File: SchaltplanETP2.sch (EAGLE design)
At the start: 62 parts, among them IC1 LM2674, IC2 ZXLD1350, IC3 ZXLD1350, IC4 ZXLD1350, IC5 ZXLD1350, M1 RN42_BLUETOOTH, T1 BUK98150-55A, X1 TERMINAL_BLOCK_MC000036, X2 TERMINAL_BLOCK_MC000036

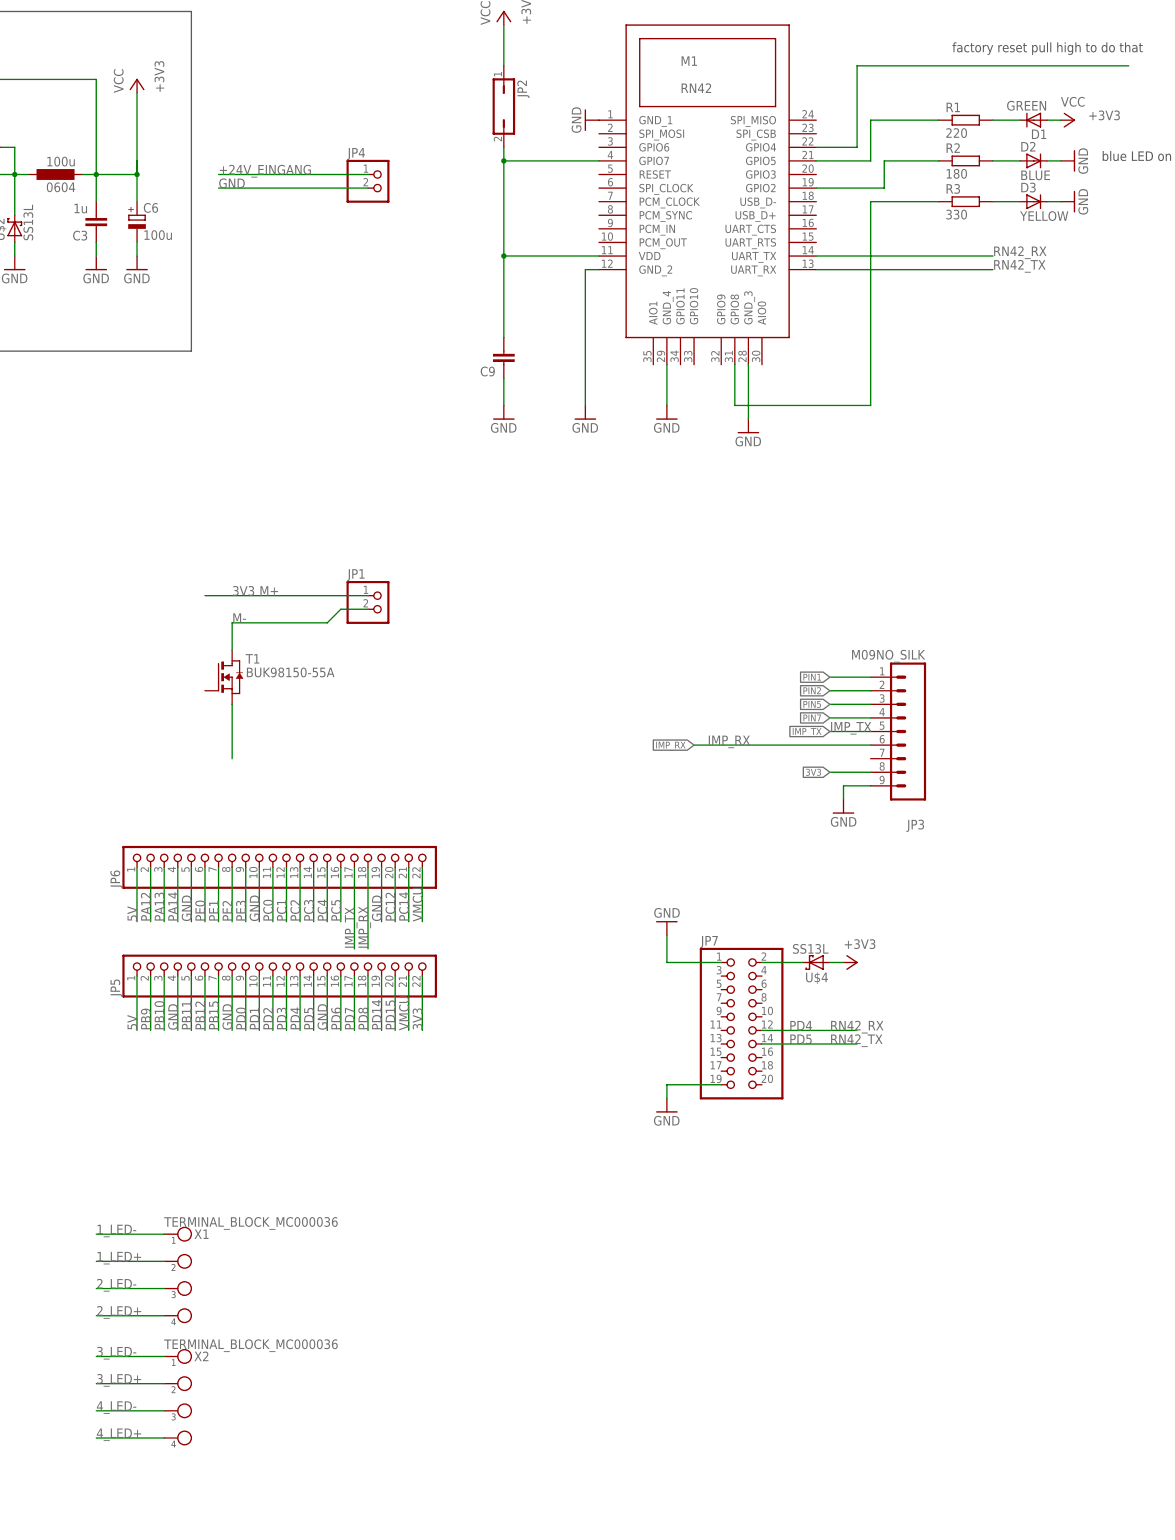
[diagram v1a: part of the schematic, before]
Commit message: connected leds directly to 24V
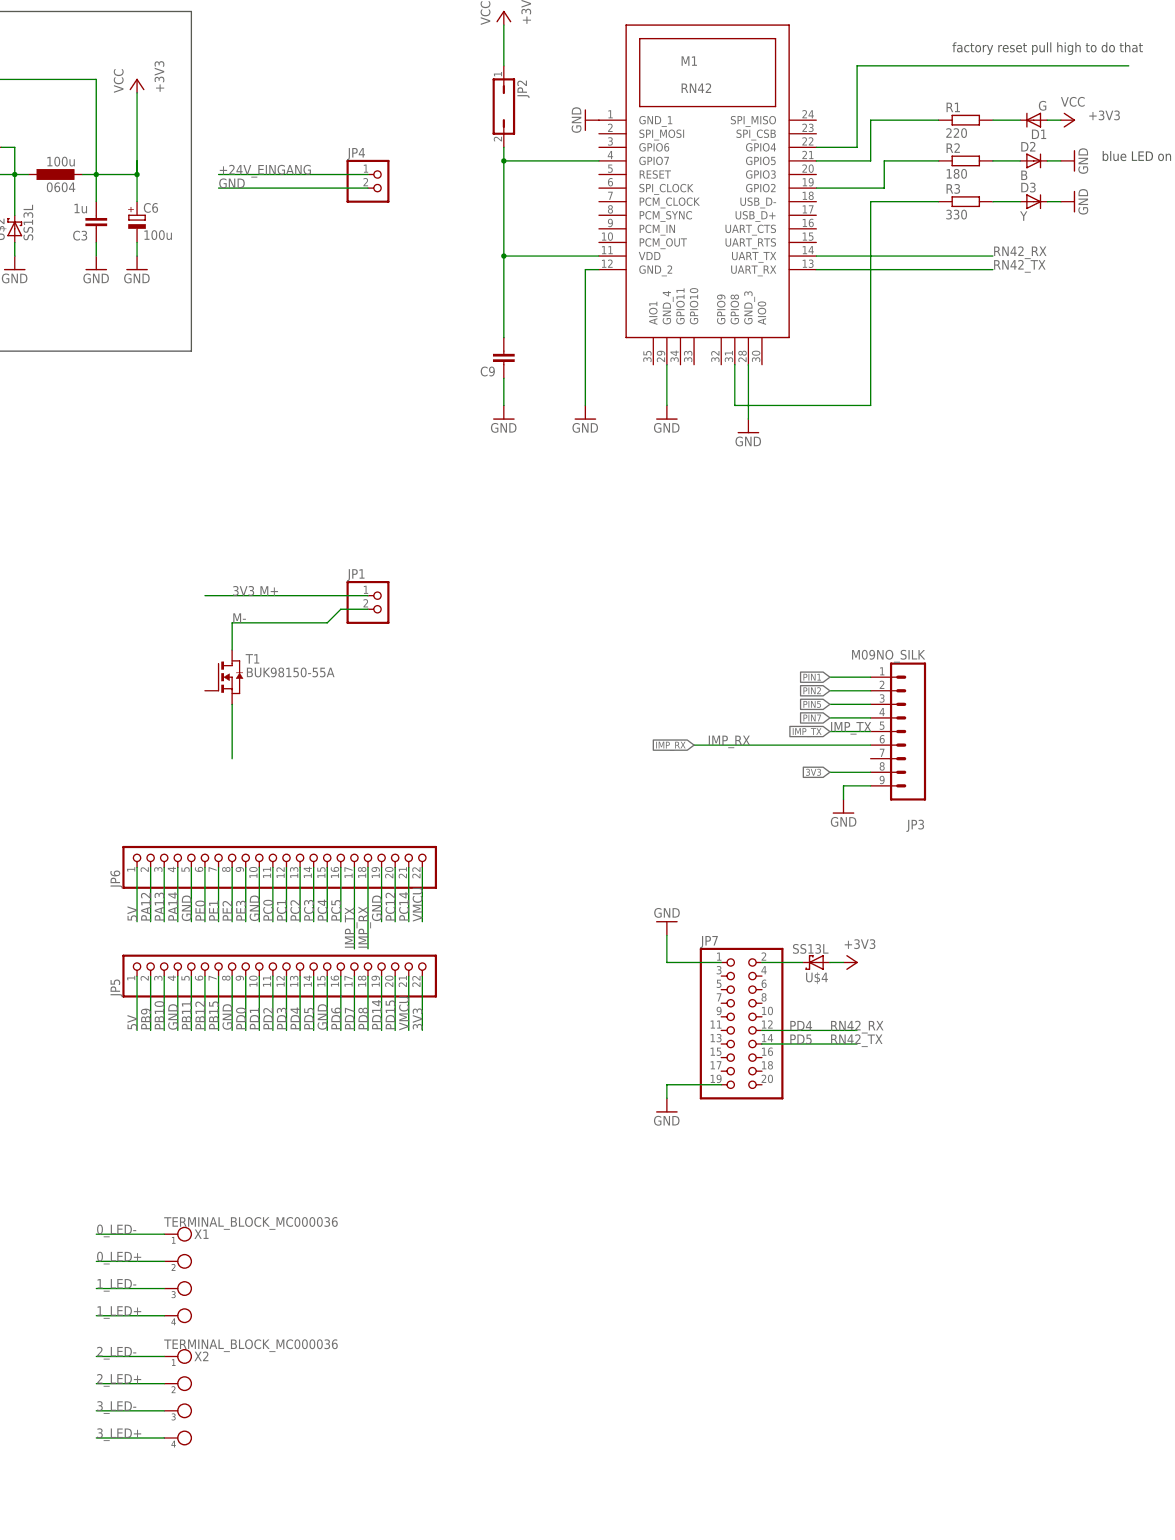
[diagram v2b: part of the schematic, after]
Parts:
- D1: value GREEN -> G
- D2: value BLUE -> B
- D3: value YELLOW -> Y
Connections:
- removed net 4_LED+: X2.4
- removed net 4_LED-: X2.3
- removed net VCC: C10.1, C13.1, C16.1, C19.1, IC2.VIN, IC3.VIN, IC4.VIN, IC5.VIN, R10.1, R4.1, R6.1, R8.1, U$5.C, U$6.C, U$7.C, U$8.C
- net +24V: now also C10.1, C13.1, C16.1, C19.1, IC2.VIN, IC3.VIN, IC4.VIN, IC5.VIN, R10.1, R4.1, R6.1, R8.1, U$5.C, U$6.C, U$7.C, U$8.C
- net 0_LED+: now also X1.2
- net 0_LED-: now also X1.1
- net 1_LED+: now also X1.4; no longer X1.2
- net 1_LED-: now also X1.3; no longer X1.1
- net 2_LED+: now also X2.2; no longer X1.4
- net 2_LED-: now also X2.1; no longer X1.3
- net 3_LED+: now also X2.4; no longer X2.2
- net 3_LED-: now also X2.3; no longer X2.1

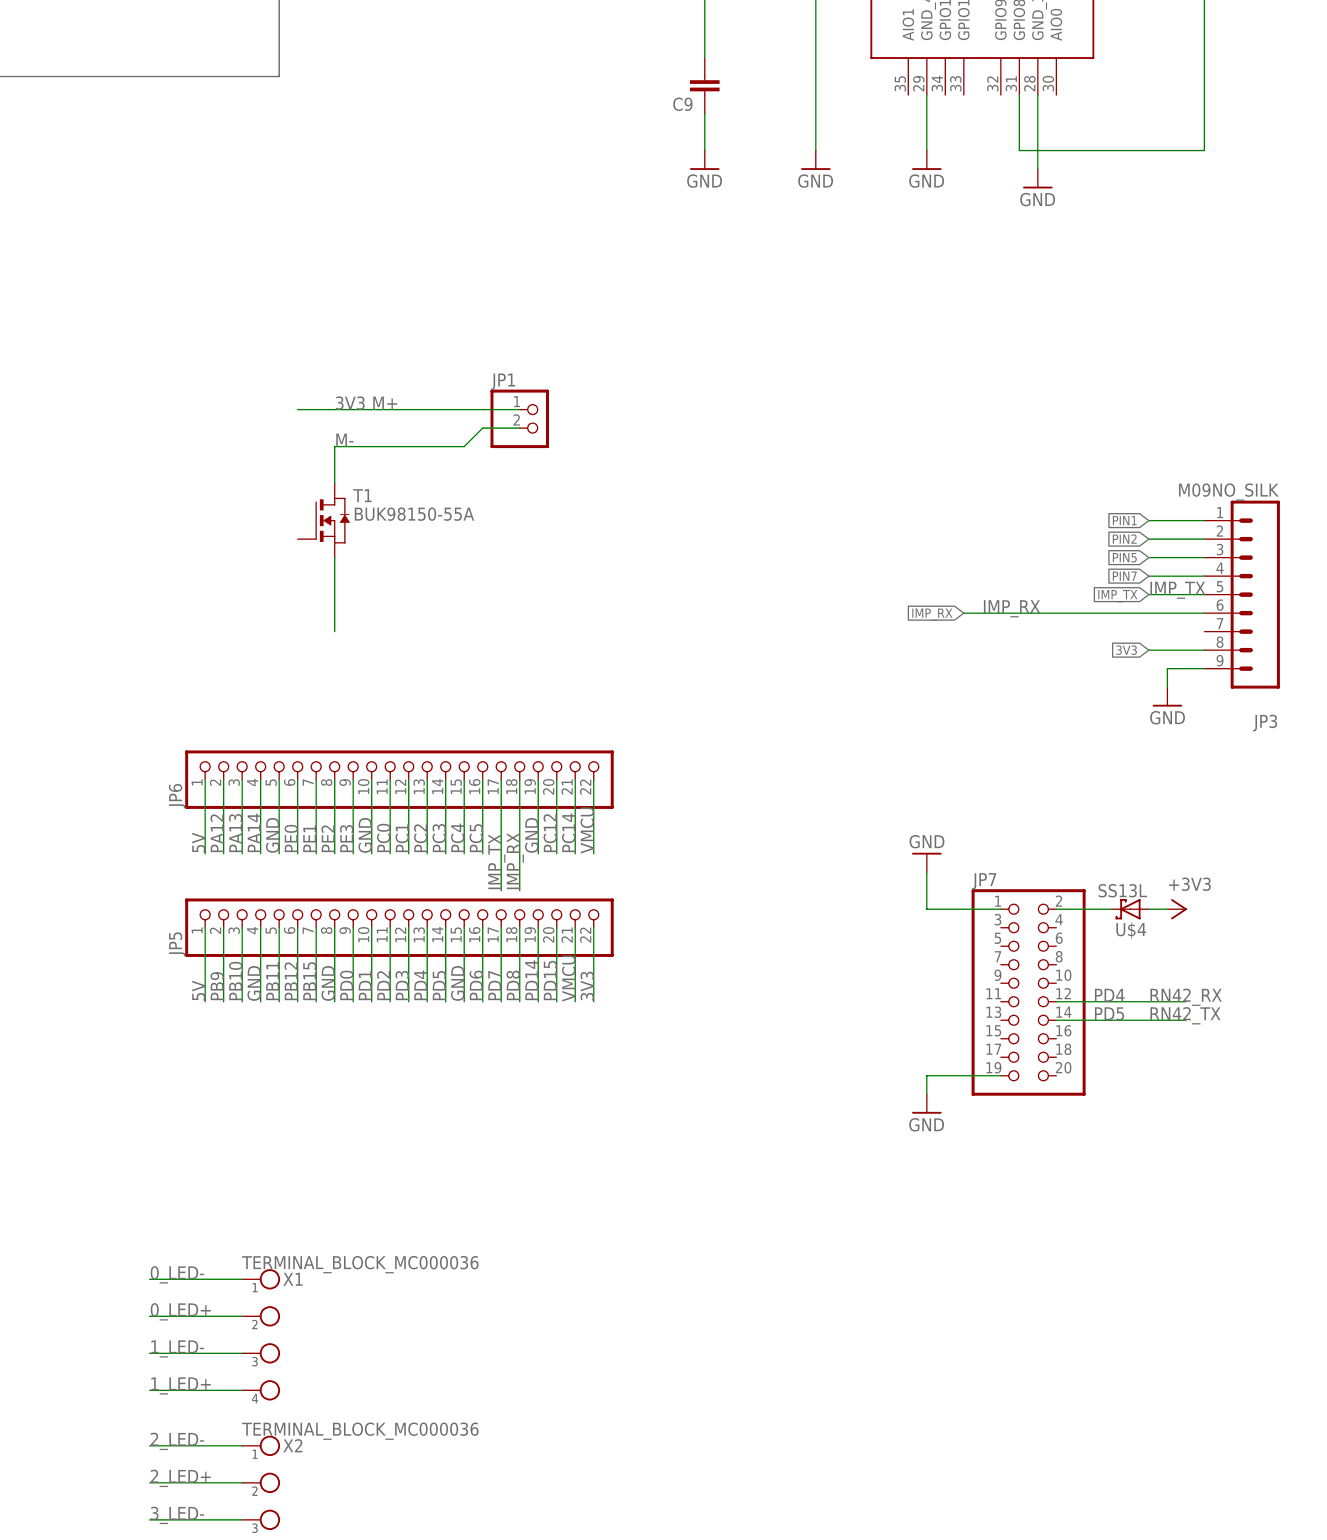
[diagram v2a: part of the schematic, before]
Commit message: added diode to motor additional pinheader for screw terminal
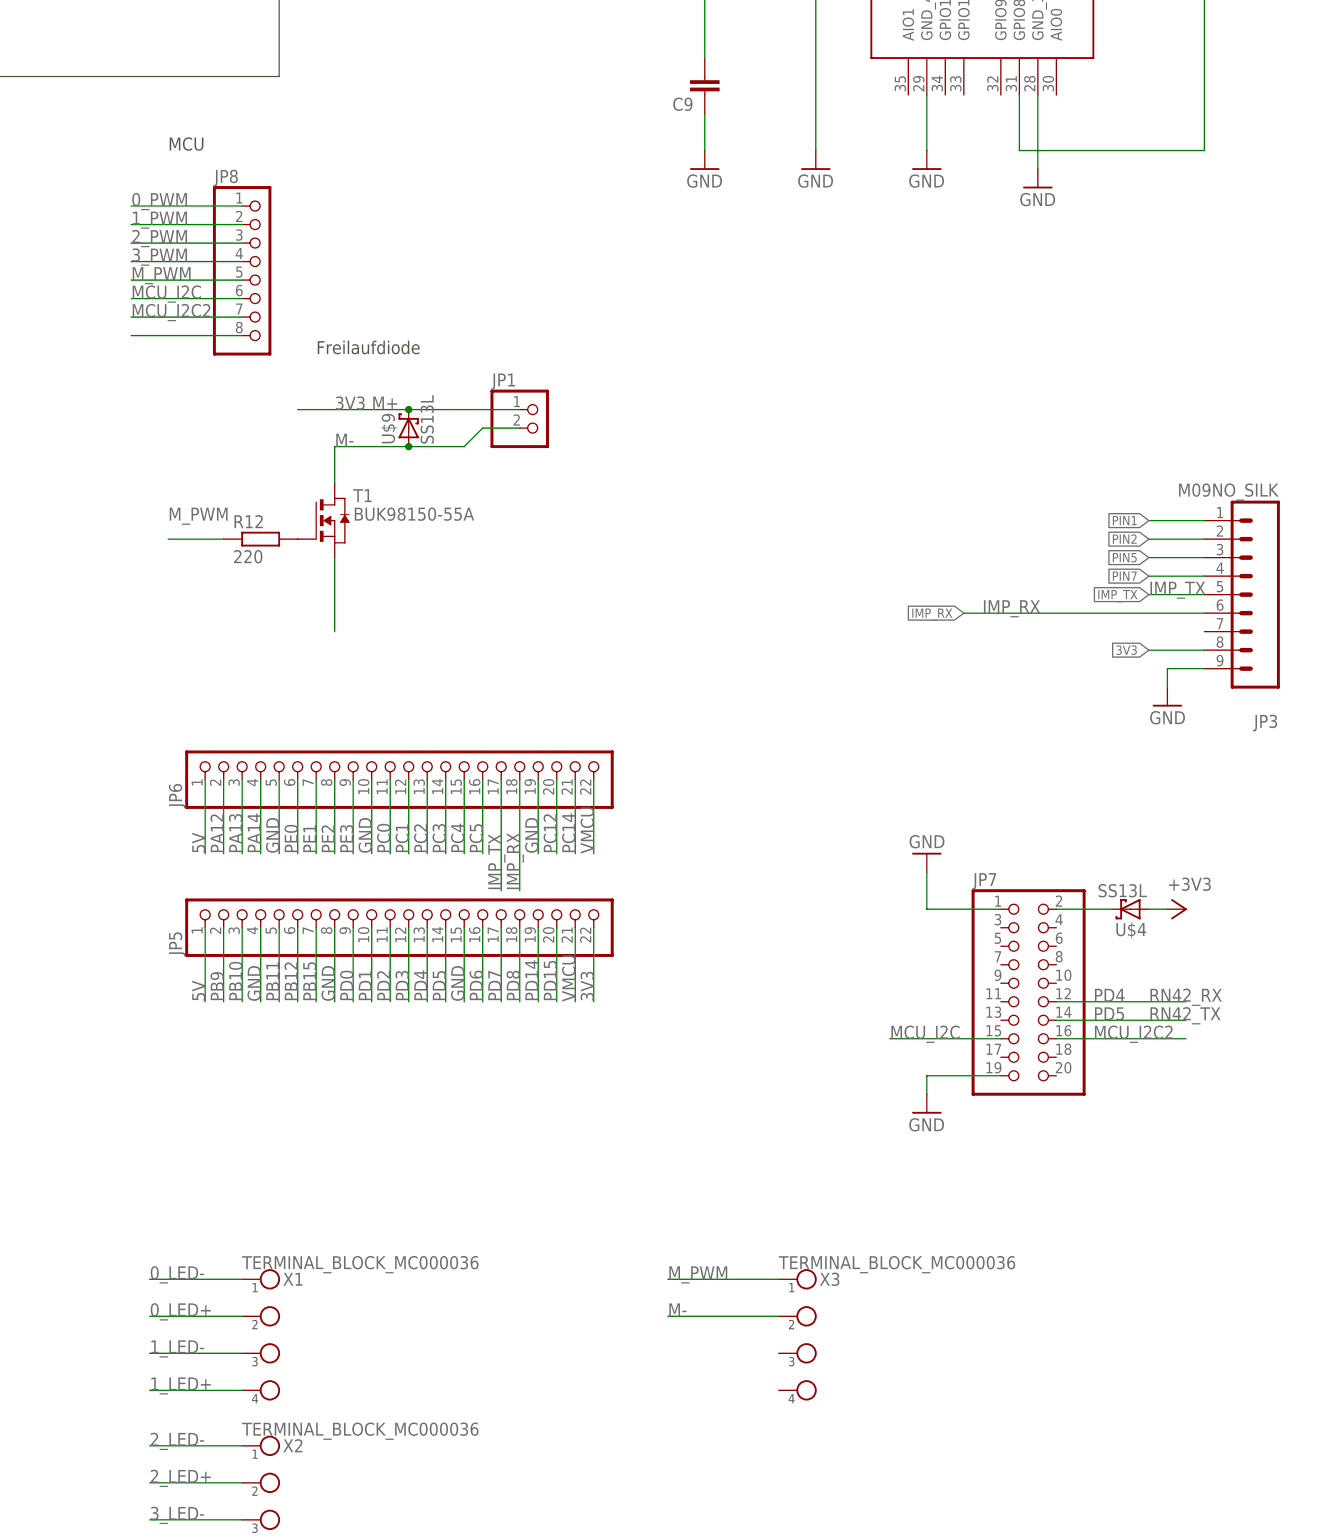
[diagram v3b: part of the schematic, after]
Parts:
- added JP8: (no value), adafruit:PINHD-1X8CLEANBIG
- added R12: 220, rcl:R-EU_M0805
- added U$9: SS13L, Moodlight:SS13L
- added X3: TERMINAL_BLOCK_MC000036, Moodlight:TERMINAL_BLOCK_MC000036
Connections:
- new net MCU_I2C: JP7.15, JP8.6
- new net MCU_I2C2: JP7.16, JP8.7
- new net M_PWM: JP8.5, R12.1, X3.1
- new net N$1: R12.2, T1.G
- new net N$28: JP8.8
- net 0_PWM: now also JP8.1
- net 1_PWM: now also JP8.2
- net 2_PWM: now also JP8.3
- net 3V3: now also U$9.C
- net 3_PWM: now also JP8.4
- net M-: now also U$9.A, X3.2
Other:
- note added: "Freilaufdiode"
- note added: "MCU"
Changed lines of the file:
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@@
 <part name="X2" library="Moodlight" deviceset="TERMINAL_BLOCK_MC000036" device=""/>
 <part name="JP4" library="pinhead" deviceset="PINHD-1X2" device=""/>
+<part name="U$9" library="Moodlight" deviceset="SS13L" device=""/>
+<part name="JP8" library="adafruit" deviceset="PINHD-1X8" device="CLEANBIG"/>
+<part name="R12" library="rcl" deviceset="R-EU_" device="M0805" value="220"/>
+<part name="X3" library="Moodlight" deviceset="TERMINAL_BLOCK_MC000036" device=""/>
 </parts>
 <sheets>
@@
 <text x="246.38" y="111.76" size="1.778" layer="97">blue LED on means connected</text>
 <text x="218.44" y="132.08" size="1.778" layer="97">factory reset pull high to do that</text>
+<text x="81.28" y="38.1" size="1.778" layer="97">Freilaufdiode</text>
+<text x="60.96" y="66.04" size="1.778" layer="97">MCU</text>
 </plain>
 <instances>
@@
 <instance part="X2" gate="1" x="73.66" y="-111.76"/>
 <instance part="JP4" gate="G$1" x="111.76" y="106.68"/>
+<instance part="U$9" gate="G$1" x="93.98" y="27.94" rot="R90"/>
+<instance part="JP8" gate="G$1" x="73.66" y="50.8"/>
+<instance part="R12" gate="G$1" x="73.66" y="12.7"/>
+<instance part="X3" gate="1" x="147.32" y="-88.9"/>
 </instances>
 <busses>
@@
 <segment>
 <pinref part="JP1" gate="G$1" pin="1"/>
-<wire x1="109.22" y1="30.48" x2="78.74" y2="30.48" width="0.1524" layer="91"/>
+<wire x1="109.22" y1="30.48" x2="93.98" y2="30.48" width="0.1524" layer="91"/>
 <label x="83.82" y="30.48" size="1.778" layer="95"/>
+<pinref part="U$9" gate="G$1" pin="C"/>
+<wire x1="93.98" y1="30.48" x2="78.74" y2="30.48" width="0.1524" layer="91"/>
+<junction x="93.98" y="30.48"/>
 </segment>
 </net>
@@
 <wire x1="-48.26" y1="7.62" x2="-63.5" y2="7.62" width="0.1524" layer="91"/>
 </segment>
+<segment>
+<pinref part="JP8" gate="G$1" pin="1"/>
+<wire x1="71.12" y1="58.42" x2="55.88" y2="58.42" width="0.1524" layer="91"/>
+<label x="55.88" y="58.42" size="1.778" layer="95"/>
+</segment>
 </net>
 <net name="N$13" class="0">
@@
 <label x="-60.96" y="-76.2" size="1.778" layer="95"/>
 </segment>
+<segment>
+<pinref part="JP8" gate="G$1" pin="2"/>
+<wire x1="71.12" y1="55.88" x2="55.88" y2="55.88" width="0.1524" layer="91"/>
+<label x="55.88" y="55.88" size="1.778" layer="95"/>
+</segment>
 </net>
 <net name="2_PWM" class="0">
@@
 <label x="-60.96" y="-160.02" size="1.778" layer="95"/>
 </segment>
+<segment>
+<pinref part="JP8" gate="G$1" pin="3"/>
+<wire x1="71.12" y1="53.34" x2="55.88" y2="53.34" width="0.1524" layer="91"/>
+<label x="55.88" y="53.34" size="1.778" layer="95"/>
+</segment>
 </net>
 <net name="3_PWM" class="0">
@@
 <wire x1="-48.26" y1="-243.84" x2="-60.96" y2="-243.84" width="0.1524" layer="91"/>
 <label x="-60.96" y="-243.84" size="1.778" layer="95"/>
+</segment>
+<segment>
+<pinref part="JP8" gate="G$1" pin="4"/>
+<wire x1="71.12" y1="50.8" x2="55.88" y2="50.8" width="0.1524" layer="91"/>
+<label x="55.88" y="50.8" size="1.778" layer="95"/>
 </segment>
 </net>
@@
 <wire x1="109.22" y1="27.94" x2="104.14" y2="27.94" width="0.1524" layer="91"/>
 <wire x1="104.14" y1="27.94" x2="101.6" y2="25.4" width="0.1524" layer="91"/>
-<wire x1="101.6" y1="25.4" x2="83.82" y2="25.4" width="0.1524" layer="91"/>
+<wire x1="101.6" y1="25.4" x2="93.98" y2="25.4" width="0.1524" layer="91"/>
 <label x="83.82" y="25.4" size="1.778" layer="95"/>
 <pinref part="T1" gate="G$1" pin="D"/>
+<wire x1="93.98" y1="25.4" x2="83.82" y2="25.4" width="0.1524" layer="91"/>
 <wire x1="83.82" y1="25.4" x2="83.82" y2="20.32" width="0.1524" layer="91"/>
+<pinref part="U$9" gate="G$1" pin="A"/>
+<junction x="93.98" y="25.4"/>
+</segment>
+<segment>
+<pinref part="X3" gate="1" pin="2"/>
+<wire x1="144.78" y1="-93.98" x2="129.54" y2="-93.98" width="0.1524" layer="91"/>
+<label x="129.54" y="-93.98" size="1.778" layer="95"/>
 </segment>
 </net>
@@
 </segment>
 </net>
+<net name="M_PWM" class="0">
+<segment>
+<label x="60.96" y="15.24" size="1.778" layer="95"/>
+<pinref part="R12" gate="G$1" pin="1"/>
+<wire x1="68.58" y1="12.7" x2="60.96" y2="12.7" width="0.1524" layer="91"/>
+</segment>
+<segment>
+<pinref part="JP8" gate="G$1" pin="5"/>
+<wire x1="71.12" y1="48.26" x2="55.88" y2="48.26" width="0.1524" layer="91"/>
+<label x="55.88" y="48.26" size="1.778" layer="95"/>
+</segment>
+<segment>
+<pinref part="X3" gate="1" pin="1"/>
+<wire x1="144.78" y1="-88.9" x2="129.54" y2="-88.9" width="0.1524" layer="91"/>
+<label x="129.54" y="-88.9" size="1.778" layer="95"/>
+</segment>
+</net>
+<net name="N$28" class="0">
+<segment>
+<pinref part="JP8" gate="G$1" pin="8"/>
+<wire x1="71.12" y1="40.64" x2="55.88" y2="40.64" width="0.1524" layer="91"/>
+</segment>
+</net>
+<net name="MCU_I2C2" class="0">
+<segment>
+<pinref part="JP7" gate="A" pin="16"/>
+<wire x1="182.88" y1="-55.88" x2="200.66" y2="-55.88" width="0.1524" layer="91"/>
+<label x="187.96" y="-55.88" size="1.778" layer="95"/>
+</segment>
+<segment>
+<pinref part="JP8" gate="G$1" pin="7"/>
+<wire x1="71.12" y1="43.18" x2="55.88" y2="43.18" width="0.1524" layer="91"/>
+<label x="55.88" y="43.18" size="1.778" layer="95"/>
+</segment>
+</net>
+<net name="MCU_I2C" class="0">
+<segment>
+<pinref part="JP7" gate="A" pin="15"/>
+<wire x1="175.26" y1="-55.88" x2="160.02" y2="-55.88" width="0.1524" layer="91"/>
+<label x="160.02" y="-55.88" size="1.778" layer="95"/>
+</segment>
+<segment>
+<pinref part="JP8" gate="G$1" pin="6"/>
+<wire x1="71.12" y1="45.72" x2="55.88" y2="45.72" width="0.1524" layer="91"/>
+<label x="55.88" y="45.72" size="1.778" layer="95"/>
+</segment>
+</net>
+<net name="N$1" class="0">
+<segment>
+<pinref part="T1" gate="G$1" pin="G"/>
+<pinref part="R12" gate="G$1" pin="2"/>
+</segment>
+</net>
